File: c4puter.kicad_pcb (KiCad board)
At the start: 6 copper layers, 200 x 200 mm, 184 parts, among them J1 PDI, J2 MICROSD, J7 19V 3A, J8 DEBUG, Q1 AOD4189, Q2 AOD4189, Q3 2N7002, U1 ATXMEGA8E5-MU

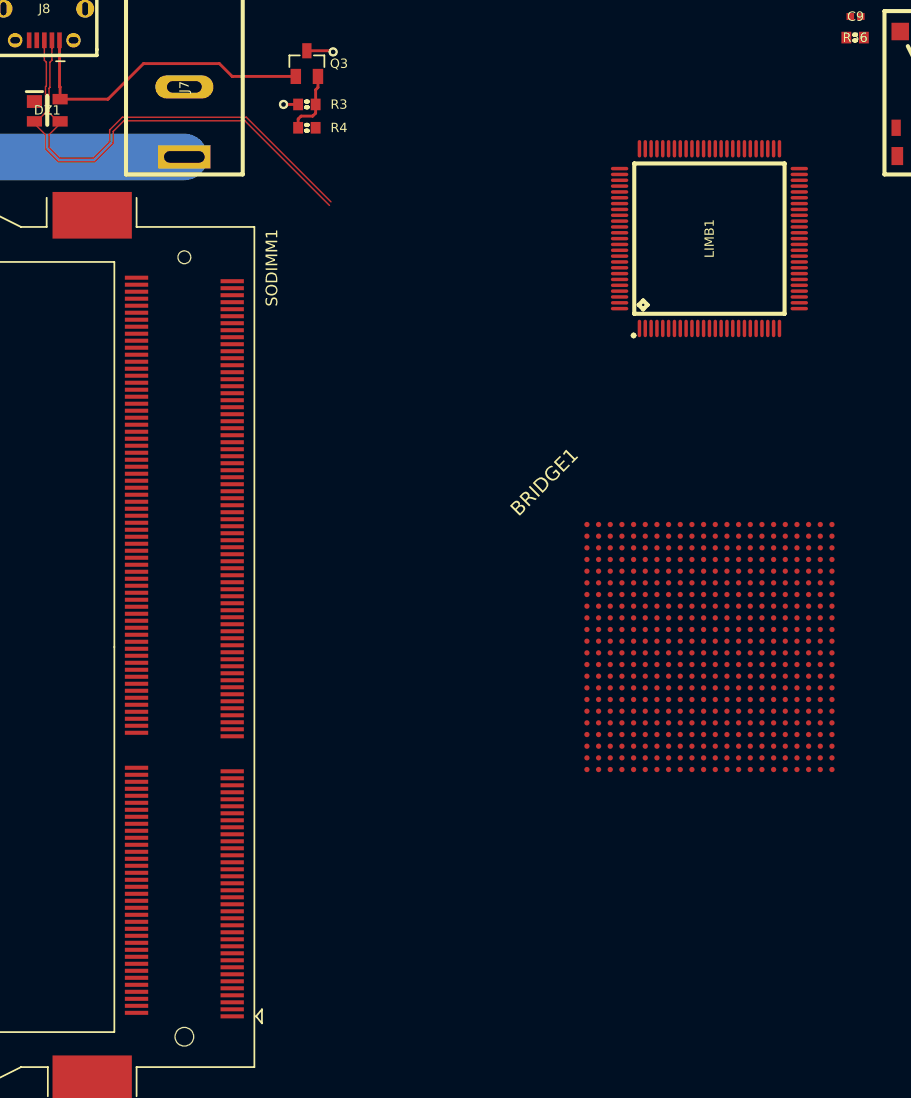
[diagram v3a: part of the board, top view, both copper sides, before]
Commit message: Reroute SDRAM after bank swap
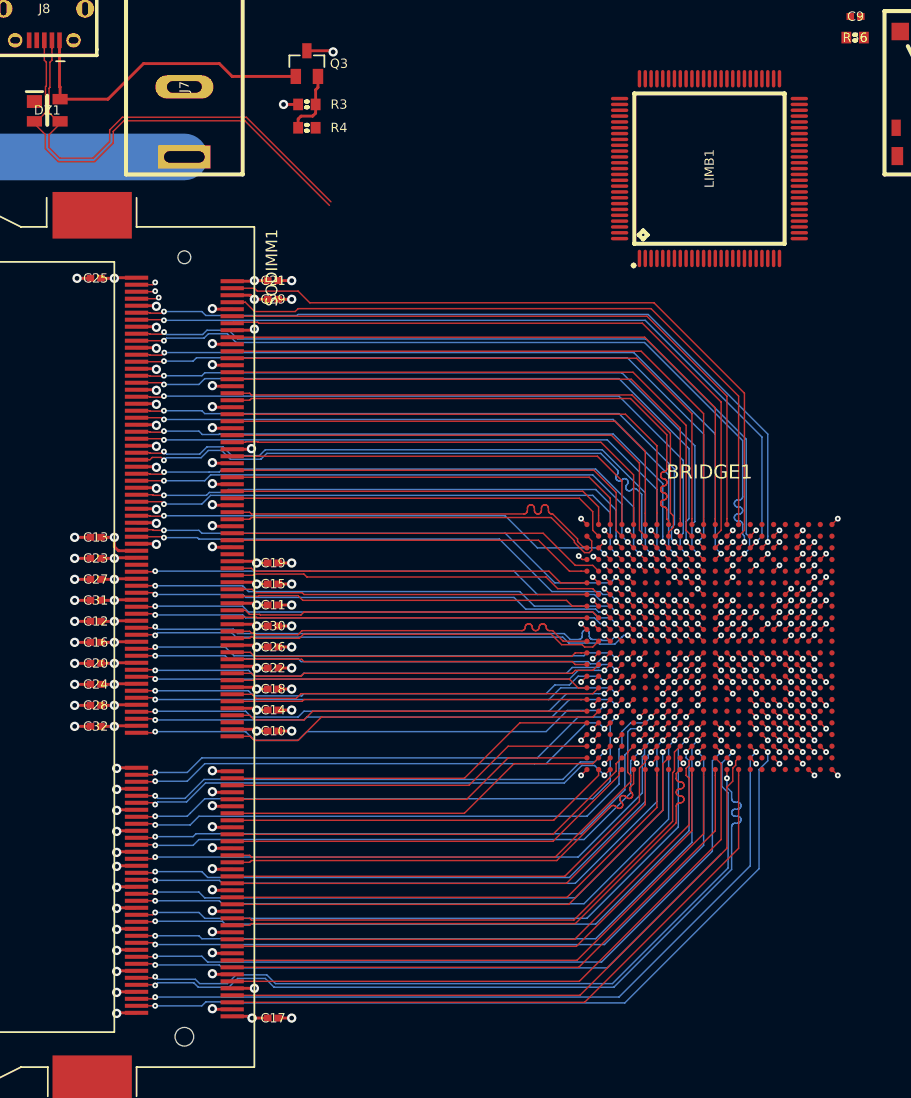
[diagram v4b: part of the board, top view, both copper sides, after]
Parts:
- added C10: 100n, IPC7351-Nominal:CAPC1005X55, F.Cu at (40.6, 63.2)
- added C11: 100n, IPC7351-Nominal:CAPC1005X55, F.Cu at (40.6, 52.4)
- added C12: 100n, IPC7351-Nominal:CAPC1005X55, F.Cu at (25.4, 53.8)
- added C13: 100n, IPC7351-Nominal:CAPC1005X55, F.Cu at (25.4, 46.6)
- added C14: 100n, IPC7351-Nominal:CAPC1005X55, F.Cu at (40.6, 61.4)
- added C15: 100n, IPC7351-Nominal:CAPC1005X55, F.Cu at (40.6, 50.6)
- added C16: 100n, IPC7351-Nominal:CAPC1005X55, F.Cu at (25.4, 55.6)
- added C17: 100n, IPC7351-Nominal:CAPC1005X55, F.Cu at (40.6, 87.8)
- added C18: 100n, IPC7351-Nominal:CAPC1005X55, F.Cu at (40.6, 59.6)
- added C19: 100n, IPC7351-Nominal:CAPC1005X55, F.Cu at (40.6, 48.8)
- added C20: 100n, IPC7351-Nominal:CAPC1005X55, F.Cu at (25.4, 57.4)
- added C21: 100n, IPC7351-Nominal:CAPC1005X55, F.Cu at (40.6, 24.6)
- added C22: 100n, IPC7351-Nominal:CAPC1005X55, F.Cu at (40.6, 57.8)
- added C23: 100n, IPC7351-Nominal:CAPC1005X55, F.Cu at (25.4, 48.4)
- added C24: 100n, IPC7351-Nominal:CAPC1005X55, F.Cu at (25.4, 59.2)
- added C25: 100n, IPC7351-Nominal:CAPC1005X55, F.Cu at (25.4, 24.4)
- added C26: 100n, IPC7351-Nominal:CAPC1005X55, F.Cu at (40.6, 56.0)
- added C27: 100n, IPC7351-Nominal:CAPC1005X55, F.Cu at (25.4, 50.2)
- added C28: 100n, IPC7351-Nominal:CAPC1005X55, F.Cu at (25.4, 61.0)
- added C29: 100n, IPC7351-Nominal:CAPC1005X55, F.Cu at (40.6, 26.2)
- added C30: 100n, IPC7351-Nominal:CAPC1005X55, F.Cu at (40.6, 54.2)
- added C31: 100n, IPC7351-Nominal:CAPC1005X55, F.Cu at (25.4, 52.0)
- added C32: 100n, IPC7351-Nominal:CAPC1005X55, F.Cu at (25.4, 62.8)
- moved LIMB1 6.00 mm to (78.0, 15.0)
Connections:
- net +1.5 renamed P1V5_RAM
- net /Power Distrib/VTT renamed PV75_VTT
- BRIDGE1 pad A10: Net-(BRIDGE1-PadA10) -> /Multibridge/A3
- BRIDGE1 pad A11: Net-(BRIDGE1-PadA11) -> /Multibridge/A1
- BRIDGE1 pad A12: Net-(BRIDGE1-PadA12) -> /Multibridge/CK0_N
- BRIDGE1 pad A14: Net-(BRIDGE1-PadA14) -> /Multibridge/A10
- BRIDGE1 pad A15: Net-(BRIDGE1-PadA15) -> /Multibridge/~WE
- BRIDGE1 pad A16: Net-(BRIDGE1-PadA16) -> /Multibridge/~CAS
- BRIDGE1 pad A17: Net-(BRIDGE1-PadA17) -> /Multibridge/~S1
- BRIDGE1 pad A18: Net-(BRIDGE1-PadA18) -> /Multibridge/DQ32
- BRIDGE1 pad A2: Net-(BRIDGE1-PadA2) -> /Multibridge/DM3
- BRIDGE1 pad A20: Net-(BRIDGE1-PadA20) -> /Multibridge/DQS4_P
- BRIDGE1 pad A21: Net-(BRIDGE1-PadA21) -> /Multibridge/DQS4_N
- BRIDGE1 pad A3: Net-(BRIDGE1-PadA3) -> /Multibridge/DQ26
- BRIDGE1 pad A5: Net-(BRIDGE1-PadA5) -> /Multibridge/DQ27
- BRIDGE1 pad A6: Net-(BRIDGE1-PadA6) -> /Multibridge/BA2
- BRIDGE1 pad A7: Net-(BRIDGE1-PadA7) -> /Multibridge/A12
- BRIDGE1 pad A8: Net-(BRIDGE1-PadA8) -> /Multibridge/A8
- BRIDGE1 pad B1: Net-(BRIDGE1-PadB1) -> /Multibridge/DQ24
- BRIDGE1 pad B10: Net-(BRIDGE1-PadB10) -> /Multibridge/A5
- BRIDGE1 pad B12: Net-(BRIDGE1-PadB12) -> /Multibridge/CK0_P
- BRIDGE1 pad B14: Net-(BRIDGE1-PadB14) -> /Multibridge/BA0
- BRIDGE1 pad B16: Net-(BRIDGE1-PadB16) -> /Multibridge/A13
- BRIDGE1 pad B18: Net-(BRIDGE1-PadB18) -> /Multibridge/DQ33
- BRIDGE1 pad B2: Net-(BRIDGE1-PadB2) -> /Multibridge/DQ25
- BRIDGE1 pad B21: Net-(BRIDGE1-PadB21) -> /Multibridge/DQ34
- BRIDGE1 pad B22: Net-(BRIDGE1-PadB22) -> /Multibridge/DQ35
- BRIDGE1 pad B6: Net-(BRIDGE1-PadB6) -> /Multibridge/CKE0
- BRIDGE1 pad B8: Net-(BRIDGE1-PadB8) -> /Multibridge/A9
- BRIDGE1 pad C1: Net-(BRIDGE1-PadC1) -> /Multibridge/DQS3_N
- BRIDGE1 pad C10: Net-(BRIDGE1-PadC10) -> /Multibridge/A6
- BRIDGE1 pad C11: Net-(BRIDGE1-PadC11) -> /Multibridge/A2
- BRIDGE1 pad C13: Net-(BRIDGE1-PadC13) -> /Multibridge/BA1
- BRIDGE1 pad C14: Net-(BRIDGE1-PadC14) -> /Multibridge/~S0
- BRIDGE1 pad C15: Net-(BRIDGE1-PadC15) -> /Multibridge/ODT1
- BRIDGE1 pad C19: Net-(BRIDGE1-PadC19) -> /Multibridge/DM4
- BRIDGE1 pad C22: Net-(BRIDGE1-PadC22) -> /Multibridge/DQ40
- BRIDGE1 pad C3: Net-(BRIDGE1-PadC3) -> /Multibridge/DQS3_P
- BRIDGE1 pad C5: Net-(BRIDGE1-PadC5) -> /Multibridge/DQ30
- BRIDGE1 pad C6: Net-(BRIDGE1-PadC6) -> /Multibridge/DQ31
- BRIDGE1 pad C7: Net-(BRIDGE1-PadC7) -> /Multibridge/CKE1
- BRIDGE1 pad C8: Net-(BRIDGE1-PadC8) -> /Multibridge/A14
- BRIDGE1 pad C9: Net-(BRIDGE1-PadC9) -> /Multibridge/A7
- BRIDGE1 pad D1: Net-(BRIDGE1-PadD1) -> /Multibridge/DQ18
- BRIDGE1 pad D10: Net-(BRIDGE1-PadD10) -> /Multibridge/A4
- BRIDGE1 pad D11: Net-(BRIDGE1-PadD11) -> /Multibridge/A0
- BRIDGE1 pad D12: Net-(BRIDGE1-PadD12) -> /Multibridge/CK1_N
- BRIDGE1 pad D13: Net-(BRIDGE1-PadD13) -> /Multibridge/~RAS
- BRIDGE1 pad D14: Net-(BRIDGE1-PadD14) -> /Multibridge/ODT0
- BRIDGE1 pad D15: Net-(BRIDGE1-PadD15) -> /Multibridge/DQ36
- BRIDGE1 pad D17: Net-(BRIDGE1-PadD17) -> /Multibridge/DQ37
- BRIDGE1 pad D19: Net-(BRIDGE1-PadD19) -> /Multibridge/DQ38
- BRIDGE1 pad D2: Net-(BRIDGE1-PadD2) -> /Multibridge/DQ19
- BRIDGE1 pad D20: Net-(BRIDGE1-PadD20) -> /Multibridge/DQ39
- BRIDGE1 pad D21: Net-(BRIDGE1-PadD21) -> /Multibridge/DQ41
- BRIDGE1 pad D22: Net-(BRIDGE1-PadD22) -> /Multibridge/DM5
- BRIDGE1 pad D6: Net-(BRIDGE1-PadD6) -> /Multibridge/DQ29
- BRIDGE1 pad D7: Net-(BRIDGE1-PadD7) -> /Multibridge/A15
- BRIDGE1 pad D8: Net-(BRIDGE1-PadD8) -> /Multibridge/A11
- BRIDGE1 pad E1: Net-(BRIDGE1-PadE1) -> /Multibridge/DQS2_N
- BRIDGE1 pad E12: Net-(BRIDGE1-PadE12) -> /Multibridge/CK1_P
- BRIDGE1 pad E20: Net-(BRIDGE1-PadE20) -> /Multibridge/DQ44
- BRIDGE1 pad E22: Net-(BRIDGE1-PadE22) -> /Multibridge/DQ42
- BRIDGE1 pad E3: Net-(BRIDGE1-PadE3) -> /Multibridge/DQS2_P
- BRIDGE1 pad F1: Net-(BRIDGE1-PadF1) -> /Multibridge/DQ16
- BRIDGE1 pad F19: Net-(BRIDGE1-PadF19) -> /Multibridge/DQ45
- BRIDGE1 pad F2: Net-(BRIDGE1-PadF2) -> /Multibridge/DQ17
- BRIDGE1 pad F20: Net-(BRIDGE1-PadF20) -> /Multibridge/DQS5_N
- BRIDGE1 pad F21: Net-(BRIDGE1-PadF21) -> /Multibridge/DQ43
- BRIDGE1 pad F22: Net-(BRIDGE1-PadF22) -> /Multibridge/DQ48
- BRIDGE1 pad F3: Net-(BRIDGE1-PadF3) -> /Multibridge/DQ22
- BRIDGE1 pad F5: Net-(BRIDGE1-PadF5) -> /Multibridge/DQ23
- BRIDGE1 pad G1: Net-(BRIDGE1-PadG1) -> /Multibridge/DQ11
- BRIDGE1 pad G19: Net-(BRIDGE1-PadG19) -> /Multibridge/DQS5_P
- BRIDGE1 pad G22: Net-(BRIDGE1-PadG22) -> /Multibridge/DQ49
- BRIDGE1 pad G3: Net-(BRIDGE1-PadG3) -> /Multibridge/DQ21
- BRIDGE1 pad G4: Net-(BRIDGE1-PadG4) -> /Multibridge/DM2
- BRIDGE1 pad G6: Net-(BRIDGE1-PadG6) -> /Multibridge/DQ28
- BRIDGE1 pad H19: Net-(BRIDGE1-PadH19) -> /Multibridge/DQ46
- BRIDGE1 pad H2: Net-(BRIDGE1-PadH2) -> /Multibridge/DQ10
- BRIDGE1 pad H20: Net-(BRIDGE1-PadH20) -> /Multibridge/DQ47
- BRIDGE1 pad H21: Net-(BRIDGE1-PadH21) -> /Multibridge/DQS6_P
- BRIDGE1 pad H22: Net-(BRIDGE1-PadH22) -> /Multibridge/DQS6_N
- BRIDGE1 pad H3: Net-(BRIDGE1-PadH3) -> /Multibridge/DQ15
- BRIDGE1 pad H4: Net-(BRIDGE1-PadH4) -> /Multibridge/DQ20
- BRIDGE1 pad J1: Net-(BRIDGE1-PadJ1) -> /Multibridge/DQS1_N
- BRIDGE1 pad J19: Net-(BRIDGE1-PadJ19) -> /Multibridge/DQ52
- BRIDGE1 pad J20: Net-(BRIDGE1-PadJ20) -> /Multibridge/DQ53
- BRIDGE1 pad J22: Net-(BRIDGE1-PadJ22) -> /Multibridge/DQ50
- BRIDGE1 pad J3: Net-(BRIDGE1-PadJ3) -> /Multibridge/DQS1_P
- BRIDGE1 pad J4: Net-(BRIDGE1-PadJ4) -> /Multibridge/DQ14
- BRIDGE1 pad K1: Net-(BRIDGE1-PadK1) -> /Multibridge/DQ8
- BRIDGE1 pad K19: Net-(BRIDGE1-PadK19) -> /Multibridge/DM6
- BRIDGE1 pad K2: Net-(BRIDGE1-PadK2) -> /Multibridge/DQ9
- BRIDGE1 pad K20: Net-(BRIDGE1-PadK20) -> /Multibridge/DQ54
- BRIDGE1 pad K21: Net-(BRIDGE1-PadK21) -> /Multibridge/DQ51
- BRIDGE1 pad K22: Net-(BRIDGE1-PadK22) -> /Multibridge/DQ56
- BRIDGE1 pad K3: Net-(BRIDGE1-PadK3) -> /Multibridge/DM1
- BRIDGE1 pad K4: Net-(BRIDGE1-PadK4) -> /Multibridge/SDRAM_~RST
- BRIDGE1 pad L1: Net-(BRIDGE1-PadL1) -> /Multibridge/DQ3
- BRIDGE1 pad L19: Net-(BRIDGE1-PadL19) -> /Multibridge/DQ55
- BRIDGE1 pad L20: Net-(BRIDGE1-PadL20) -> /Multibridge/DQ60
- BRIDGE1 pad L22: Net-(BRIDGE1-PadL22) -> /Multibridge/DQ57
- BRIDGE1 pad L3: Net-(BRIDGE1-PadL3) -> /Multibridge/DQ12
- BRIDGE1 pad L4: Net-(BRIDGE1-PadL4) -> /Multibridge/DQ13
- BRIDGE1 pad M1: Net-(BRIDGE1-PadM1) -> /Multibridge/DQ2
- BRIDGE1 pad M19: Net-(BRIDGE1-PadM19) -> /Multibridge/DQ61
- BRIDGE1 pad M2: Net-(BRIDGE1-PadM2) -> /Multibridge/DM0
- BRIDGE1 pad M21: Net-(BRIDGE1-PadM21) -> /Multibridge/DQ58
- BRIDGE1 pad M22: Net-(BRIDGE1-PadM22) -> /Multibridge/DM7
- BRIDGE1 pad M3: Net-(BRIDGE1-PadM3) -> /Multibridge/DQ7
- BRIDGE1 pad N1: Net-(BRIDGE1-PadN1) -> /Multibridge/DQS0_N
- BRIDGE1 pad N22: Net-(BRIDGE1-PadN22) -> /Multibridge/DQ59
- BRIDGE1 pad N3: Net-(BRIDGE1-PadN3) -> /Multibridge/DQS0_P
- BRIDGE1 pad P1: Net-(BRIDGE1-PadP1) -> /Multibridge/DQ0
- BRIDGE1 pad P19: Net-(BRIDGE1-PadP19) -> /Multibridge/DQS7_P
- BRIDGE1 pad P2: Net-(BRIDGE1-PadP2) -> /Multibridge/DQ1
- BRIDGE1 pad P20: Net-(BRIDGE1-PadP20) -> /Multibridge/DQS7_N
- BRIDGE1 pad P21: Net-(BRIDGE1-PadP21) -> /Multibridge/SA1
- BRIDGE1 pad P22: Net-(BRIDGE1-PadP22) -> /Multibridge/SA0
- BRIDGE1 pad R20: Net-(BRIDGE1-PadR20) -> /Multibridge/DQ62
- BRIDGE1 pad R3: Net-(BRIDGE1-PadR3) -> /Multibridge/DQ5
- BRIDGE1 pad T20: Net-(BRIDGE1-PadT20) -> /Multibridge/DQ63
- BRIDGE1 pad T3: Net-(BRIDGE1-PadT3) -> /Multibridge/DQ4
- SODIMM1 pad 1: /Power Distrib/VREFDQ -> PV75_VREF
- SODIMM1 pad 126: /Power Distrib/VREFCA -> PV75_VREF
- SODIMM1 pad 199: /Power Distrib/VDDSPD -> P3V3_AUX
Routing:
- net GND: track 27.2 -> 186.6 mm, vias 13 -> 147
- net /Multibridge/DQ4: track 0.00 -> 69.3 mm, vias 0 -> 2
- net /Multibridge/DQ63: track 0.00 -> 68.6 mm, vias 0 -> 2
- net /Multibridge/DQ5: track 0.00 -> 68.0 mm, vias 0 -> 2
- net /Multibridge/DQ62: track 0.00 -> 67.7 mm, vias 0 -> 2
- net /Multibridge/DQS7_N: track 0.00 -> 67.3 mm, vias 0 -> 2
- net /Multibridge/DQS7_P: track 0.00 -> 67.3 mm, vias 0 -> 2
- net /Multibridge/DQS0_N: track 0.00 -> 67.0 mm, vias 0 -> 2
- net /Multibridge/DQS0_P: track 0.00 -> 67.0 mm, vias 0 -> 2
- net /Multibridge/DQ61: track 0.00 -> 63.8 mm, vias 0 -> 2
- net /Multibridge/DQ7: track 0.00 -> 63.0 mm, vias 0 -> 2
- net /Multibridge/DQ60: track 0.00 -> 61.6 mm, vias 0 -> 2
- net /Multibridge/DQ12: track 0.00 -> 61.1 mm, vias 0 -> 2
- net /Multibridge/DQ55: track 0.00 -> 60.8 mm, vias 0 -> 2
- net /Multibridge/DQ13: track 0.00 -> 60.8 mm, vias 0 -> 2
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
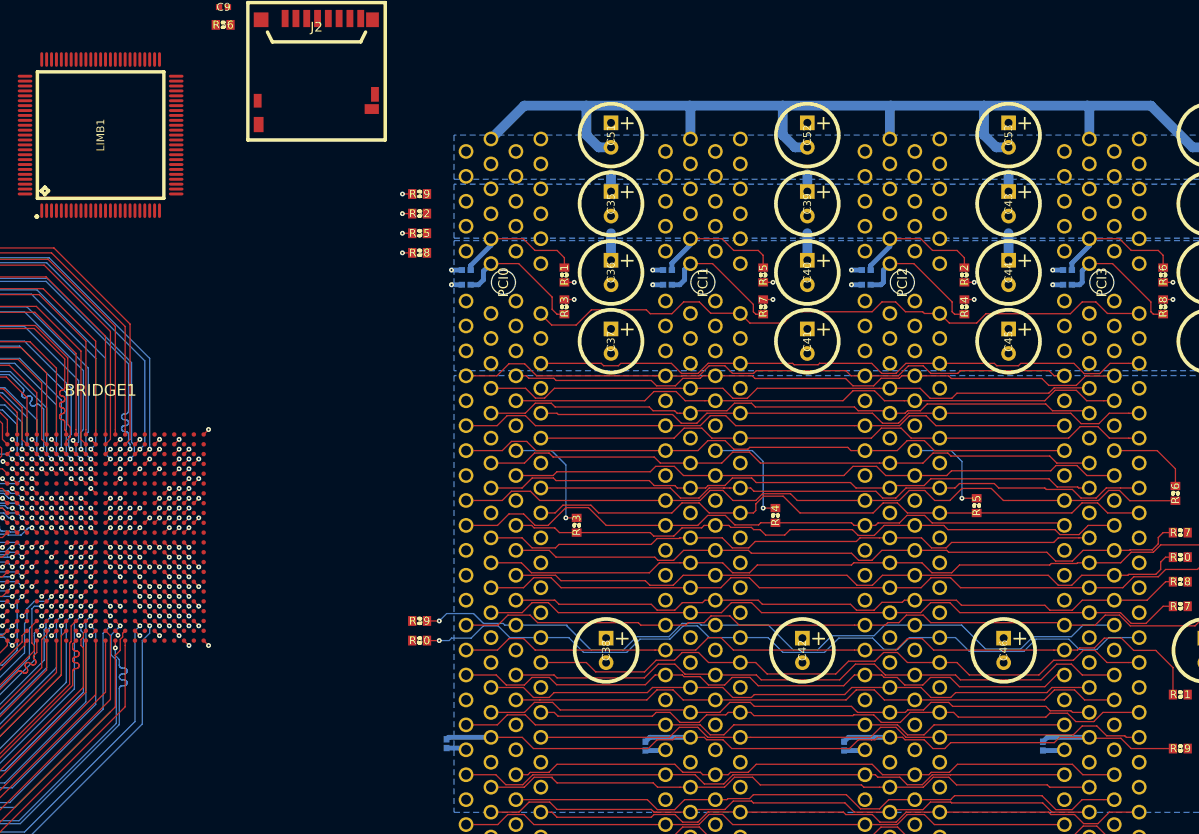
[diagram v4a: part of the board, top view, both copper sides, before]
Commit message: Route EC and half of PCI bus to bridge
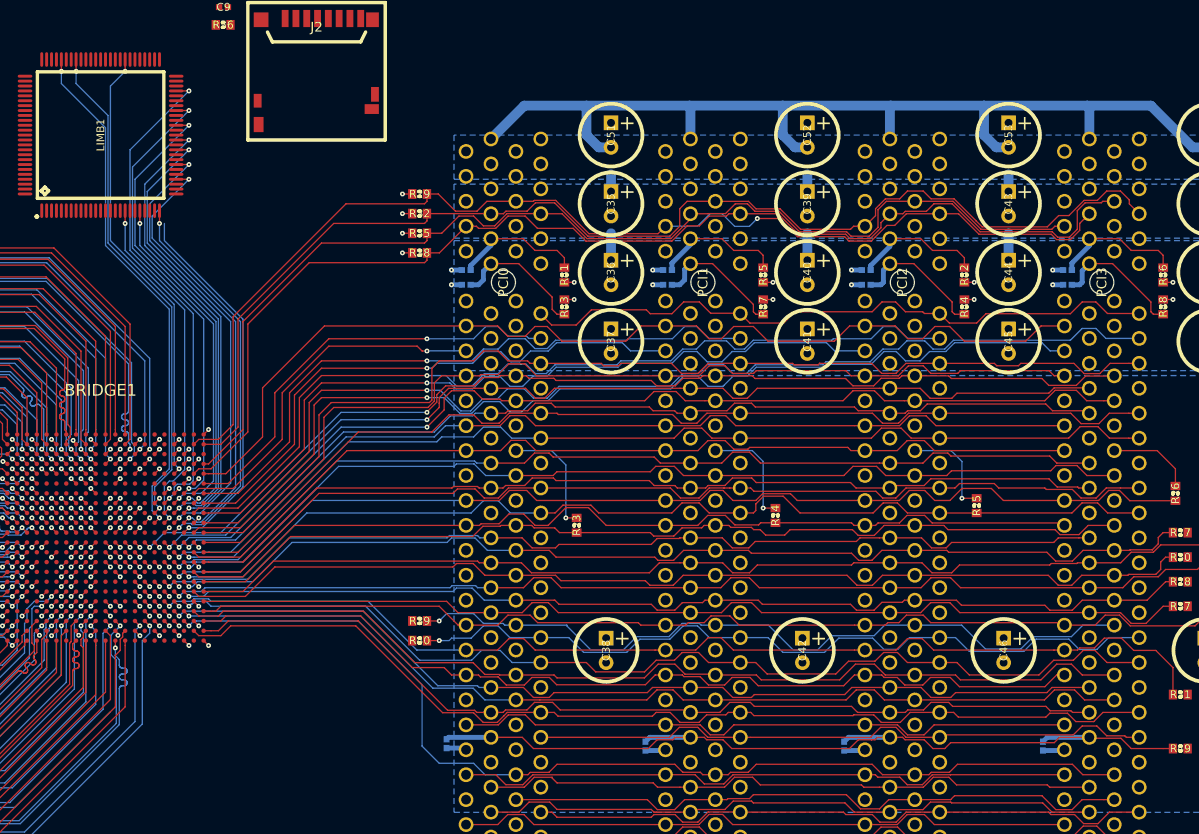
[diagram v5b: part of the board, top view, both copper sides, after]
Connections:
- net Net-(BRIDGE1-PadAA1) renamed /Multibridge/PROGRAM_B
- net Net-(BRIDGE1-PadAA20) renamed /Multibridge/DIN
- net Net-(BRIDGE1-PadAA22) renamed /Multibridge/M0
- net Net-(BRIDGE1-PadR7) renamed /PerBus/PCI_AD9
- net Net-(BRIDGE1-PadR8) renamed /PerBus/PCI_AD7
- net Net-(BRIDGE1-PadT6) renamed /Multibridge/INIT_B
- net Net-(BRIDGE1-PadT7) renamed /PerBus/PCI_AD8
- net Net-(BRIDGE1-PadU15) renamed /Multibridge/M1
- net Net-(BRIDGE1-PadY12) renamed /Multibridge/LIMBREQ
- net Net-(BRIDGE1-PadY20) renamed /Multibridge/CMPCS
- net Net-(BRIDGE1-PadY21) renamed /Multibridge/CCLK
- net Net-(BRIDGE1-PadY22) renamed /Multibridge/DONE
- BRIDGE1 pad AA10: Net-(BRIDGE1-PadAA10) -> /PerBus/PCI_CBE#3
- BRIDGE1 pad AA11: Net-(BRIDGE1-PadAA11) -> VCCO_2
- BRIDGE1 pad AA12: Net-(BRIDGE1-PadAA12) -> /PerBus/PCI_REQ#3
- BRIDGE1 pad AA14: Net-(BRIDGE1-PadAA14) -> /PerBus/PCI_GNT#2
- BRIDGE1 pad AA16: Net-(BRIDGE1-PadAA16) -> /PerBus/PCI_REQ#0
- BRIDGE1 pad AA18: Net-(BRIDGE1-PadAA18) -> /PerBus/PCI_INTD#
- BRIDGE1 pad AA2: Net-(BRIDGE1-PadAA2) -> /PerBus/PCI_AD11
- BRIDGE1 pad AA21: Net-(BRIDGE1-PadAA21) -> /PerBus/PCI_INTA#
- BRIDGE1 pad AA4: Net-(BRIDGE1-PadAA4) -> /PerBus/PCI_AD15
- BRIDGE1 pad AA6: Net-(BRIDGE1-PadAA6) -> /PerBus/PCI_TRDY#
- BRIDGE1 pad AA8: Net-(BRIDGE1-PadAA8) -> /PerBus/PCI_AD17
- BRIDGE1 pad AB10: Net-(BRIDGE1-PadAB10) -> /PerBus/PCI_AD26
- BRIDGE1 pad AB11: Net-(BRIDGE1-PadAB11) -> /PerBus/PCI_AD31
- BRIDGE1 pad AB12: Net-(BRIDGE1-PadAB12) -> /PerBus/PCI_PME#
- BRIDGE1 pad AB13: Net-(BRIDGE1-PadAB13) -> /PerBus/PCI_GNT#3
- BRIDGE1 pad AB14: Net-(BRIDGE1-PadAB14) -> /PerBus/PCI_REQ#2
- BRIDGE1 pad AB15: Net-(BRIDGE1-PadAB15) -> /PerBus/PCI_REQ#1
- BRIDGE1 pad AB16: Net-(BRIDGE1-PadAB16) -> /PerBus/PCI_GNT#1
- BRIDGE1 pad AB17: Net-(BRIDGE1-PadAB17) -> /PerBus/PCI_GNT#0
- BRIDGE1 pad AB18: Net-(BRIDGE1-PadAB18) -> /PerBus/PCI_CLK
- BRIDGE1 pad AB19: Net-(BRIDGE1-PadAB19) -> /PerBus/PCI_INTC#
- BRIDGE1 pad AB2: Net-(BRIDGE1-PadAB2) -> /PerBus/PCI_AD12
- BRIDGE1 pad AB21: Net-(BRIDGE1-PadAB21) -> /PerBus/PCI_INTB#
- BRIDGE1 pad AB3: Net-(BRIDGE1-PadAB3) -> /PerBus/PCI_CBE#1
- BRIDGE1 pad AB4: Net-(BRIDGE1-PadAB4) -> /PerBus/PCI_PERR#
- BRIDGE1 pad AB5: Net-(BRIDGE1-PadAB5) -> /PerBus/PCI_LOCK#
- BRIDGE1 pad AB6: Net-(BRIDGE1-PadAB6) -> /PerBus/PCI_IRDY#
- BRIDGE1 pad AB7: Net-(BRIDGE1-PadAB7) -> /PerBus/PCI_AD16
- BRIDGE1 pad AB8: Net-(BRIDGE1-PadAB8) -> /PerBus/PCI_AD20
- BRIDGE1 pad AB9: Net-(BRIDGE1-PadAB9) -> /PerBus/PCI_AD21
- BRIDGE1 pad T11: Net-(BRIDGE1-PadT11) -> /PerBus/PCI_AD30
- BRIDGE1 pad U13: Net-(BRIDGE1-PadU13) -> /Multibridge/LIMBNCS
- BRIDGE1 pad U14: Net-(BRIDGE1-PadU14) -> /Multibridge/LIMBNRD
- BRIDGE1 pad U6: Net-(BRIDGE1-PadU6) -> /PerBus/PCI_AD10
- BRIDGE1 pad V11: Net-(BRIDGE1-PadV11) -> /PerBus/PCI_AD29
- BRIDGE1 pad V13: Net-(BRIDGE1-PadV13) -> /EC/A15
- BRIDGE1 pad V15: Net-(BRIDGE1-PadV15) -> /EC/D1
- BRIDGE1 pad V5: Net-(BRIDGE1-PadV5) -> /PerBus/PCI_SERR#
- BRIDGE1 pad V7: Net-(BRIDGE1-PadV7) -> /PerBus/PCI_CBE#2
- BRIDGE1 pad W10: Net-(BRIDGE1-PadW10) -> /PerBus/PCI_AD25
- BRIDGE1 pad W11: Net-(BRIDGE1-PadW11) -> /PerBus/PCI_AD28
- BRIDGE1 pad W12: Net-(BRIDGE1-PadW12) -> /EC/D0
- BRIDGE1 pad W13: Net-(BRIDGE1-PadW13) -> /EC/D6
- BRIDGE1 pad W14: Net-(BRIDGE1-PadW14) -> /EC/D4
- BRIDGE1 pad W15: Net-(BRIDGE1-PadW15) -> /EC/D3
- BRIDGE1 pad W18: Net-(BRIDGE1-PadW18) -> /Multibridge/LIMBNWE
- BRIDGE1 pad W4: Net-(BRIDGE1-PadW4) -> /PerBus/PCI_AD14
- BRIDGE1 pad W6: Net-(BRIDGE1-PadW6) -> /PerBus/PCI_DEVSEL#
- BRIDGE1 pad W8: Net-(BRIDGE1-PadW8) -> /PerBus/PCI_AD19
- BRIDGE1 pad W9: Net-(BRIDGE1-PadW9) -> /PerBus/PCI_AD23
- BRIDGE1 pad Y10: Net-(BRIDGE1-PadY10) -> /PerBus/PCI_AD24
- BRIDGE1 pad Y11: Net-(BRIDGE1-PadY11) -> /PerBus/PCI_AD27
- BRIDGE1 pad Y13: Net-(BRIDGE1-PadY13) -> /EC/D7
- BRIDGE1 pad Y14: Net-(BRIDGE1-PadY14) -> /EC/D5
- BRIDGE1 pad Y15: Net-(BRIDGE1-PadY15) -> /Multibridge/LIMBNWAIT
- BRIDGE1 pad Y16: Net-(BRIDGE1-PadY16) -> /EC/D2
- BRIDGE1 pad Y3: Net-(BRIDGE1-PadY3) -> /PerBus/PCI_CBE#0
- BRIDGE1 pad Y4: Net-(BRIDGE1-PadY4) -> /PerBus/PCI_AD13
- BRIDGE1 pad Y5: Net-(BRIDGE1-PadY5) -> /PerBus/PCI_PAR
- BRIDGE1 pad Y6: Net-(BRIDGE1-PadY6) -> /PerBus/PCI_STOP#
- BRIDGE1 pad Y7: Net-(BRIDGE1-PadY7) -> /PerBus/PCI_FRAME#
- BRIDGE1 pad Y8: Net-(BRIDGE1-PadY8) -> /PerBus/PCI_AD18
- BRIDGE1 pad Y9: Net-(BRIDGE1-PadY9) -> /PerBus/PCI_AD22
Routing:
- net /PerBus/PCI_INTB#: track 0.00 -> 123.8 mm
- net /PerBus/PCI_INTD#: track 0.00 -> 120.8 mm
- net /PerBus/PCI_INTA#: track 0.00 -> 117.7 mm, vias 0 -> 1
- net /PerBus/PCI_INTC#: track 0.00 -> 114.0 mm
- net /PerBus/PCI_GNT#3: track 0.00 -> 110.9 mm, vias 0 -> 1
- net /PerBus/PCI_REQ#3: track 0.00 -> 103.8 mm, vias 0 -> 1
- net /PerBus/PCI_CLK: track 0.00 -> 103.6 mm
- net /PerBus/PCI_GNT#2: track 0.00 -> 89.7 mm, vias 0 -> 1
- net /PerBus/PCI_REQ#2: track 0.00 -> 80.0 mm, vias 0 -> 1
- net /PerBus/PCI_GNT#1: track 0.00 -> 66.0 mm, vias 0 -> 1
- net /PerBus/PCI_REQ#1: track 0.00 -> 58.0 mm, vias 0 -> 1
- net /Multibridge/LIMBNCS: track 0.00 -> 53.0 mm, vias 0 -> 2
- net /Multibridge/LIMBNRD: track 0.00 -> 51.4 mm, vias 0 -> 2
- net /EC/D1: track 0.00 -> 50.4 mm, vias 0 -> 2
- net /EC/D3: track 0.00 -> 48.1 mm, vias 0 -> 2
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
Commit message: Finish routing PCI
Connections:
- BRIDGE1 pad R11: Net-(BRIDGE1-PadR11) -> /PerBus/PCI_AD27
- BRIDGE1 pad R7: /PerBus/PCI_AD9 -> /PerBus/PCI_AD10
- BRIDGE1 pad R8: /PerBus/PCI_AD7 -> /PerBus/PCI_AD14
- BRIDGE1 pad R9: Net-(BRIDGE1-PadR9) -> /PerBus/PCI_AD19
- BRIDGE1 pad T11: /PerBus/PCI_AD30 -> /PerBus/PCI_AD25
- BRIDGE1 pad T7: /PerBus/PCI_AD8 -> /PerBus/PCI_CBE#0
- BRIDGE1 pad U6: /PerBus/PCI_AD10 -> /PerBus/PCI_AD08
- BRIDGE1 pad U9: Net-(BRIDGE1-PadU9) -> /PerBus/PCI_FRAME#
- BRIDGE1 pad V11: /PerBus/PCI_AD29 -> /PerBus/PCI_AD24
- BRIDGE1 pad V13: /EC/A15 -> /EC/D0
- BRIDGE1 pad V15: /EC/D1 -> /Multibridge/LIMBNWAIT
- BRIDGE1 pad V5: /PerBus/PCI_SERR# -> /PerBus/PCI_AD04
- BRIDGE1 pad V7: /PerBus/PCI_CBE#2 -> /PerBus/PCI_AD07
- BRIDGE1 pad V9: Net-(BRIDGE1-PadV9) -> /PerBus/PCI_DEVSEL#
- BRIDGE1 pad W10: /PerBus/PCI_AD25 -> /PerBus/PCI_AD18
- BRIDGE1 pad W11: /PerBus/PCI_AD28 -> /PerBus/PCI_AD23
- BRIDGE1 pad W12: /EC/D0 -> /PerBus/PCI_AD29
- BRIDGE1 pad W13: /EC/D6 -> /Multibridge/LIMBREQ
- BRIDGE1 pad W14: /EC/D4 -> /EC/D6
- BRIDGE1 pad W15: /EC/D3 -> /EC/D4
- BRIDGE1 pad W4: /PerBus/PCI_AD14 -> /PerBus/PCI_AD02
- BRIDGE1 pad W6: /PerBus/PCI_DEVSEL# -> /PerBus/PCI_AD06
- BRIDGE1 pad W8: /PerBus/PCI_AD19 -> /PerBus/PCI_AD13
- BRIDGE1 pad W9: /PerBus/PCI_AD23 -> /PerBus/PCI_SERR#
- BRIDGE1 pad Y10: /PerBus/PCI_AD24 -> /PerBus/PCI_CBE#2
- BRIDGE1 pad Y11: /PerBus/PCI_AD27 -> /PerBus/PCI_AD22
- BRIDGE1 pad Y12: /Multibridge/LIMBREQ -> /PerBus/PCI_AD28
- BRIDGE1 pad Y13: /EC/D7 -> /PerBus/PCI_AD30
- BRIDGE1 pad Y14: /EC/D5 -> /EC/D7
- BRIDGE1 pad Y15: /Multibridge/LIMBNWAIT -> /EC/D5
- BRIDGE1 pad Y16: /EC/D2 -> /EC/D3
- BRIDGE1 pad Y17: Net-(BRIDGE1-PadY17) -> /EC/D2
- BRIDGE1 pad Y18: Net-(BRIDGE1-PadY18) -> /EC/D1
- BRIDGE1 pad Y19: Net-(BRIDGE1-PadY19) -> /EC/A15
- BRIDGE1 pad Y3: /PerBus/PCI_CBE#0 -> /PerBus/PCI_AD00
- BRIDGE1 pad Y4: /PerBus/PCI_AD13 -> /PerBus/PCI_AD01
- BRIDGE1 pad Y5: /PerBus/PCI_PAR -> /PerBus/PCI_AD03
- BRIDGE1 pad Y6: /PerBus/PCI_STOP# -> /PerBus/PCI_AD05
- BRIDGE1 pad Y7: /PerBus/PCI_FRAME# -> /PerBus/PCI_AD09
- BRIDGE1 pad Y8: /PerBus/PCI_AD18 -> /PerBus/PCI_PAR
- BRIDGE1 pad Y9: /PerBus/PCI_AD22 -> /PerBus/PCI_STOP#
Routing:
- net /PerBus/PCI_AD04: track 63.9 -> 116.7 mm, vias 0 -> 1
- net /PerBus/PCI_AD02: track 63.6 -> 116.2 mm, vias 0 -> 1
- net /PerBus/PCI_AD00: track 63.8 -> 113.7 mm, vias 0 -> 1
- net /PerBus/PCI_AD06: track 64.2 -> 112.4 mm, vias 0 -> 1
- net /PerBus/PCI_AD08: track 63.4 -> 109.5 mm, vias 0 -> 1
- net /PerBus/PCI_AD07: track 63.5 -> 109.1 mm, vias 0 -> 1
- net /PerBus/PCI_AD05: track 63.6 -> 108.2 mm, vias 0 -> 1
- net /PerBus/PCI_AD01: track 63.7 -> 107.3 mm, vias 0 -> 1
- net /PerBus/PCI_AD09: track 63.6 -> 106.6 mm, vias 0 -> 1
- net /PerBus/PCI_AD03: track 63.5 -> 106.3 mm, vias 0 -> 1
- net /PerBus/PCI_AD10: track 64.2 -> 104.7 mm
- net /EC/A15: track 35.8 -> 28.7 mm
- net /PerBus/PCI_CBE#0: track 108.0 -> 114.8 mm
- net /PerBus/PCI_AD14: track 99.4 -> 105.3 mm
- net /PerBus/PCI_AD30: track 109.2 -> 104.0 mm
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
